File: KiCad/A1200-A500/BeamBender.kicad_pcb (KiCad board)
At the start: 4 copper layers, 50 x 100 mm, 82 parts, among them J1 4-1734742-0, J2 HDMI_A_1.4, J3 STX-3501-3N, J4 Phoenix_Contact, J5 Conn_01x01, J6 Conn_02x06_Odd_Even, U1 LM1117-3.3, U2 GW1NR-UV9LQ144P, U3 ADV7513BSWZ, U4 MCP1702T-1802E_CB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

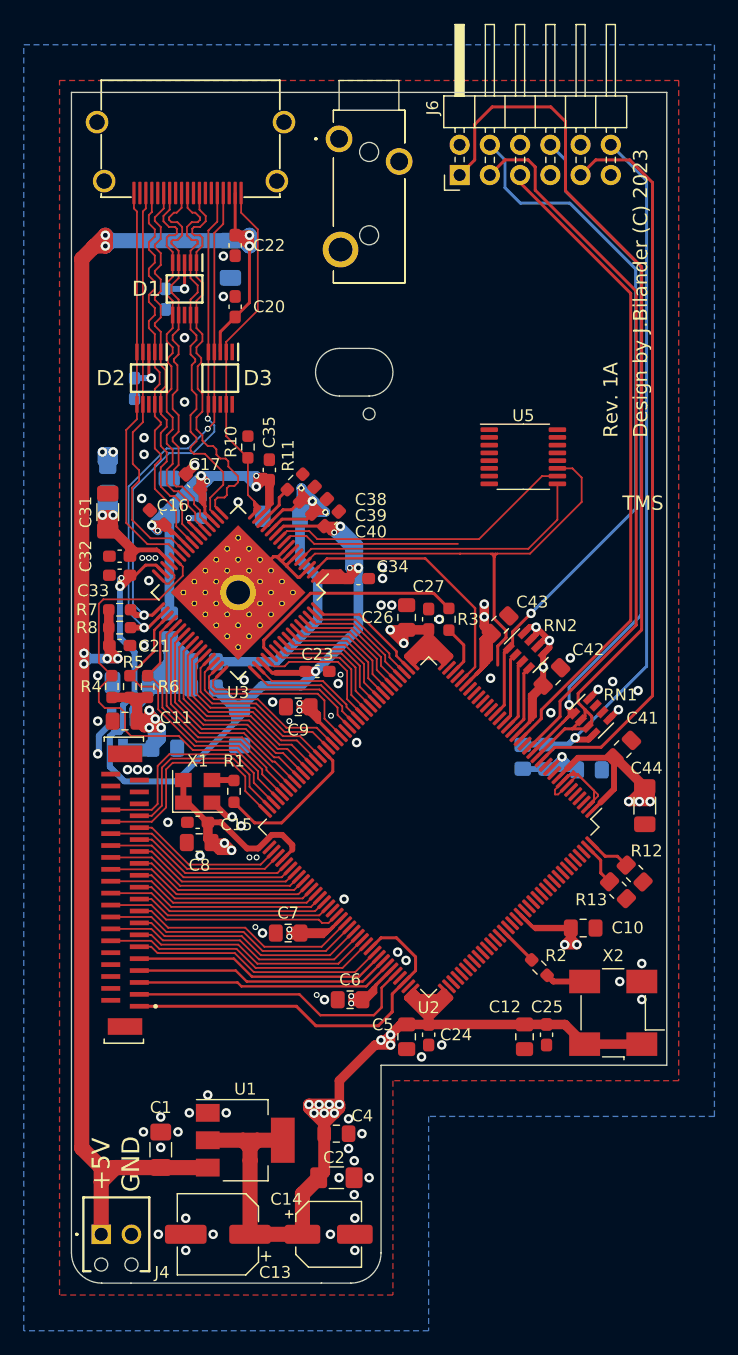
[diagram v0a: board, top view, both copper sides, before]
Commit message: added a 24.576 MHz crystal oscillator 5.0x3.2mm for Audio MCLK routed to FPGA pin 98 (GCLKT_2)
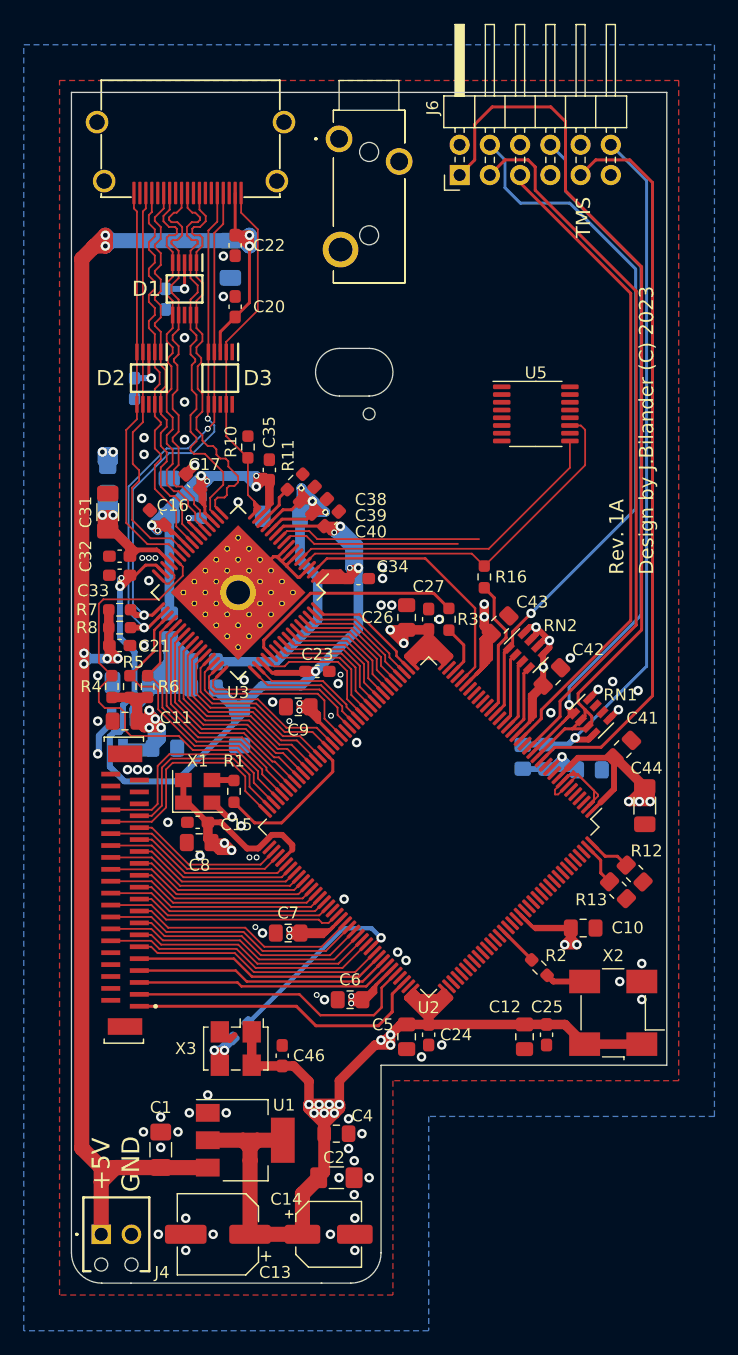
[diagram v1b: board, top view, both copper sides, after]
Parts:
- added C46: 0.01uF (0603), Capacitor_SMD:C_0603_1608Metric_Pad1.08x0.95mm_HandSolder, F.Cu at (115.8, 121.1)
- added R15: 22, Resistor_SMD:R_0603_1608Metric_Pad0.98x0.95mm_HandSolder, B.Cu at (112.3, 119.0)
- added R16: 22, Resistor_SMD:R_0603_1608Metric_Pad0.98x0.95mm_HandSolder, F.Cu at (132.8, 80.9)
- added X3: 5.0x3.2mm, Oscillator:Oscillator_SMD_TXC_7C-4Pin_5.0x3.2mm_HandSoldering, F.Cu at (111.9, 120.5)
- moved U5 3.75 mm to (137.1, 67.2)
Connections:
- U2 pad 98: C14M_3V3 -> XTAL_24.576M
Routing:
- net XTAL_24.576M: track 0.00 -> 16.0 mm, vias 0 -> 1
- net Net-(R16-Pad1): track 0.00 -> 11.5 mm
- net 3V3: track 296.1 -> 306.2 mm
- net LRCLK: track 26.0 -> 17.3 mm
- net MCLK: track 40.8 -> 32.2 mm
- net Net-(R15-Pad1): track 0.00 -> 7.48 mm, vias 0 -> 2
- net C14M_3V3: track 32.7 -> 25.3 mm
- net I2S0: track 25.9 -> 28.0 mm
- net GND: track 38.8 -> 39.5 mm, vias 76 -> 75

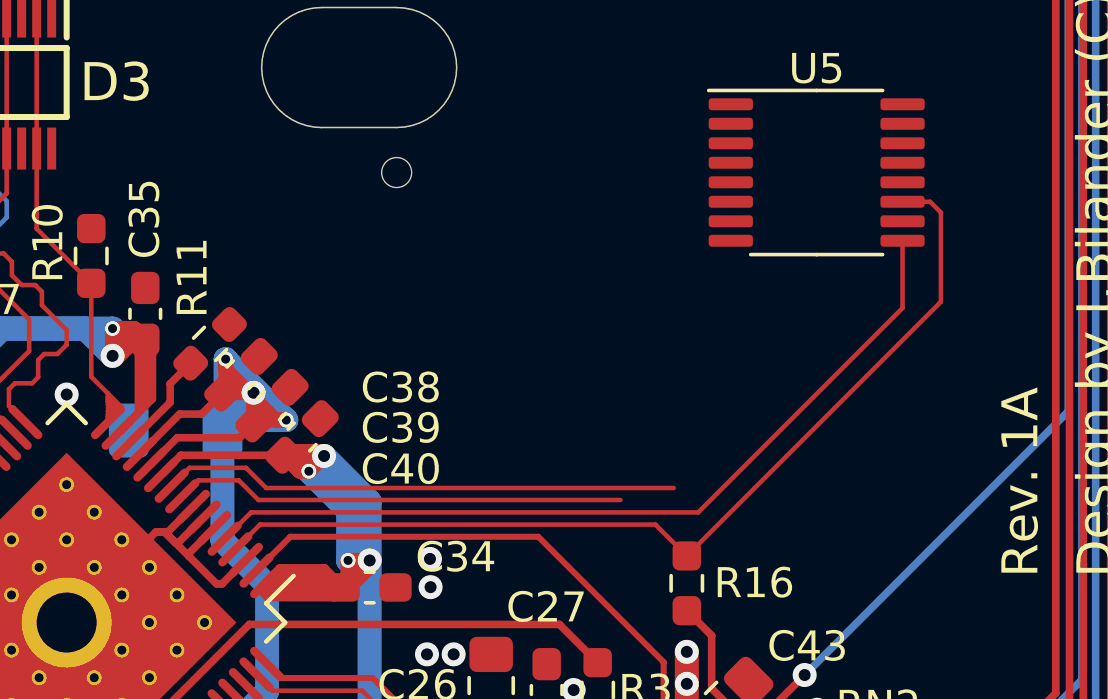
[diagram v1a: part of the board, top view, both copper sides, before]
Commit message: Added series resistors to BCLK, LRCLK and I2S0 audio lines.
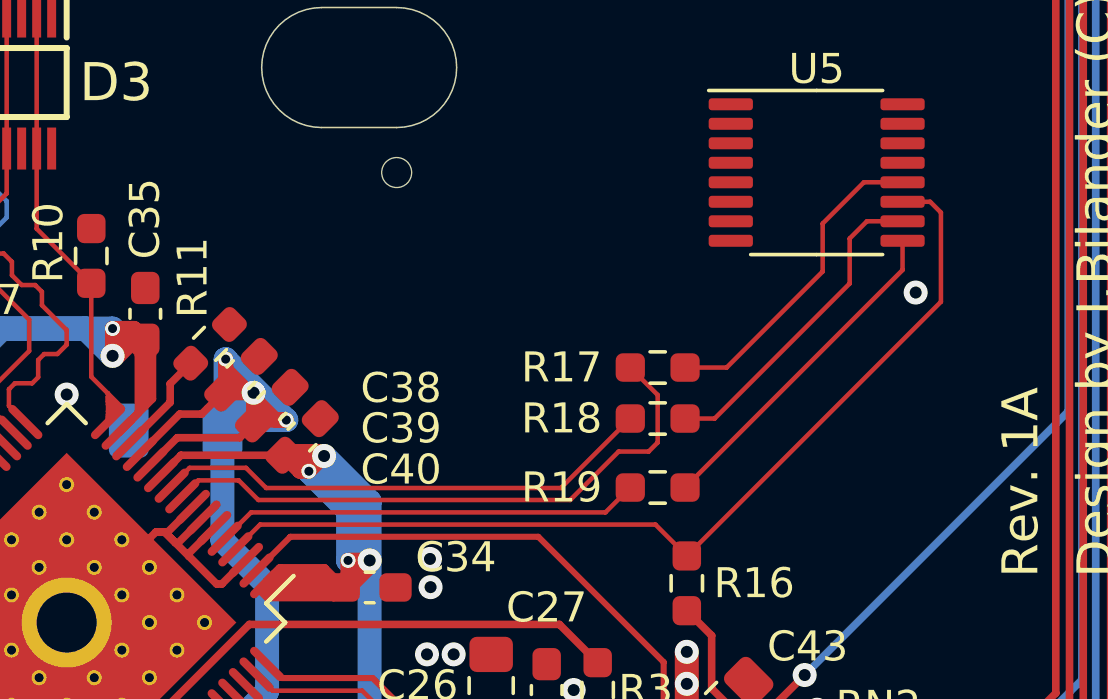
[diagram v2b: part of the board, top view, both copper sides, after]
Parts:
- added R17: 22, Resistor_SMD:R_0603_1608Metric_Pad0.98x0.95mm_HandSolder, F.Cu at (131.8, 73.7)
- added R18: 22, Resistor_SMD:R_0603_1608Metric_Pad0.98x0.95mm_HandSolder, F.Cu at (131.8, 75.4)
- added R19: 22, Resistor_SMD:R_0603_1608Metric_Pad0.98x0.95mm_HandSolder, F.Cu at (131.8, 77.7)
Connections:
- U5 pad 10: LRCLK -> Net-(R18-Pad1)
- U5 pad 12: BCLK -> Net-(R17-Pad1)
- U5 pad 9: I2S0 -> Net-(R19-Pad1)
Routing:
- net I2S0: track 28.0 -> 14.2 mm
- net Net-(R19-Pad1): track 0.00 -> 11.2 mm
- net Net-(R18-Pad1): track 0.00 -> 10.9 mm
- net Net-(R17-Pad1): track 0.00 -> 10.7 mm
- net BCLK: track 15.1 -> 20.0 mm
- net GND: vias 75 -> 76

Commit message: assigned the audio Left and Right channels to 3.5mm phono jack (STX-3501-3N) and to ADC-chip (AK5720)
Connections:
- J3 pad 1: L_AUDIO -> GND
- J3 pad 2: R_AUDIO -> L_AUDIO
- J3 pad 3: GND -> R_AUDIO
- U5 pad 2: Net-(U5-Pad2) -> R_AUDIO
- U5 pad 3: Net-(U5-Pad3) -> L_AUDIO

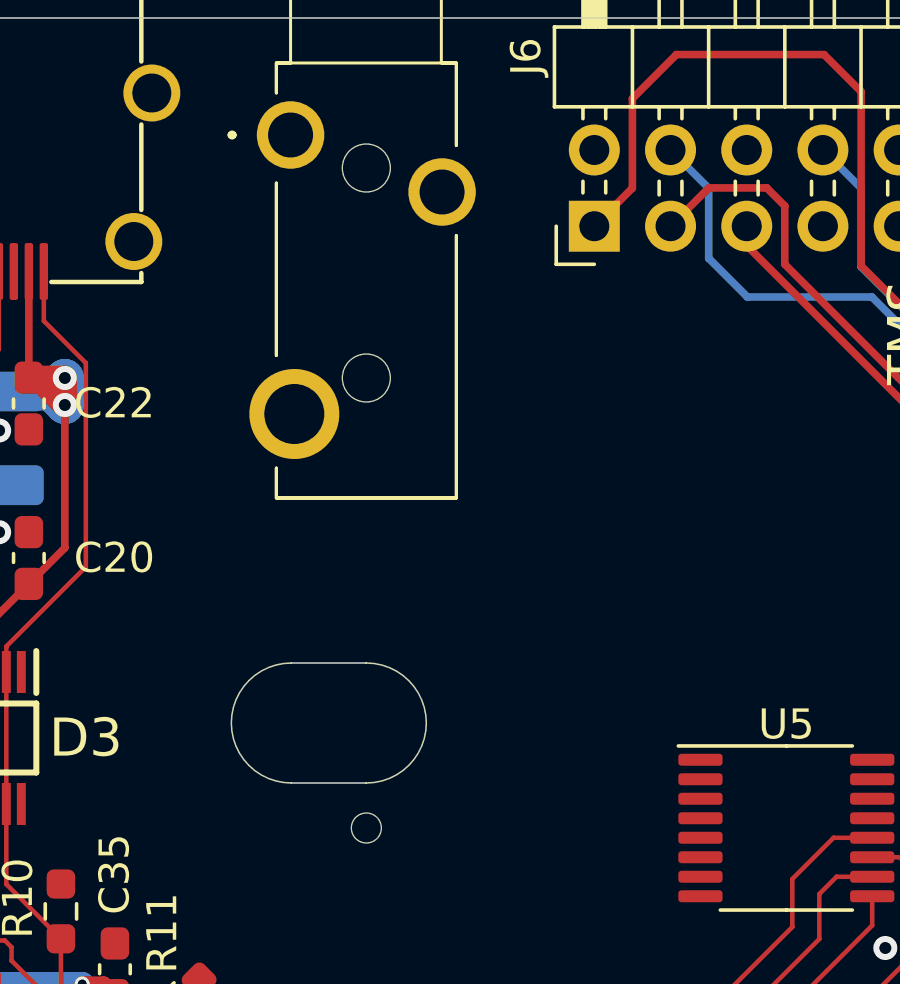
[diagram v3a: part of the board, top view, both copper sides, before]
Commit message: Added coupling caps for analogue left and right channel to inputs on ADC-chip (AK5720VT)
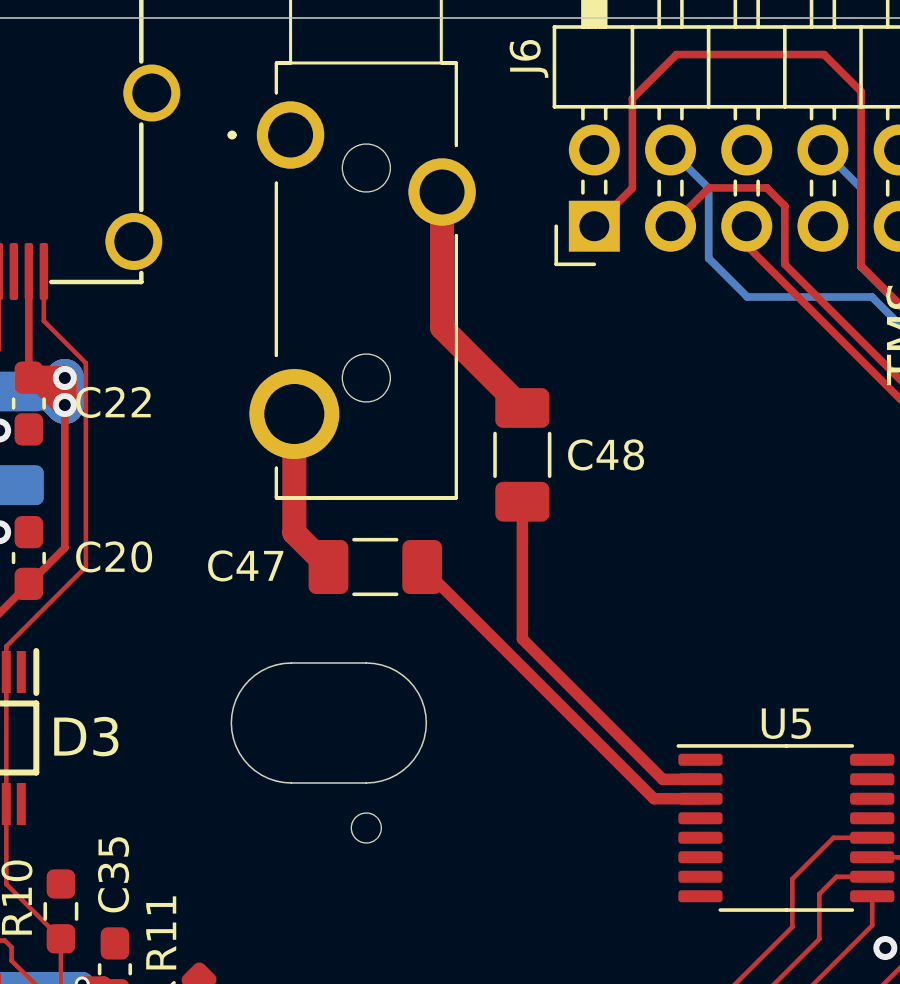
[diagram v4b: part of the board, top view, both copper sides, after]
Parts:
- added C47: 10uF (1206), Capacitor_SMD:C_1206_3216Metric_Pad1.33x1.80mm_HandSolder, F.Cu at (123.4, 58.5)
- added C48: 10uF (1206), Capacitor_SMD:C_1206_3216Metric_Pad1.33x1.80mm_HandSolder, F.Cu at (128.3, 54.8)
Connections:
- U5 pad 2: R_AUDIO -> Net-(C48-Pad2)
- U5 pad 3: L_AUDIO -> Net-(C47-Pad2)
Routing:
- net Net-(C47-Pad2): track 0.00 -> 12.5 mm
- net Net-(C48-Pad2): track 0.00 -> 12.4 mm
- net R_AUDIO: track 0.00 -> 8.31 mm
- net L_AUDIO: track 0.00 -> 5.57 mm

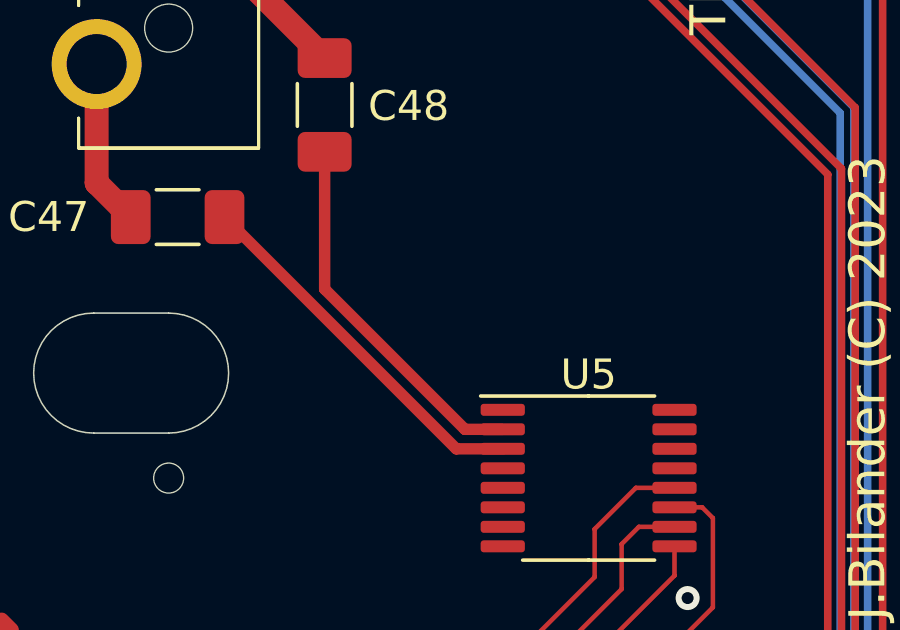
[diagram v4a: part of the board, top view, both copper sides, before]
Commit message: Added a 0.47uF cap for ADC-chip VCOM pin (Voltage Reference)
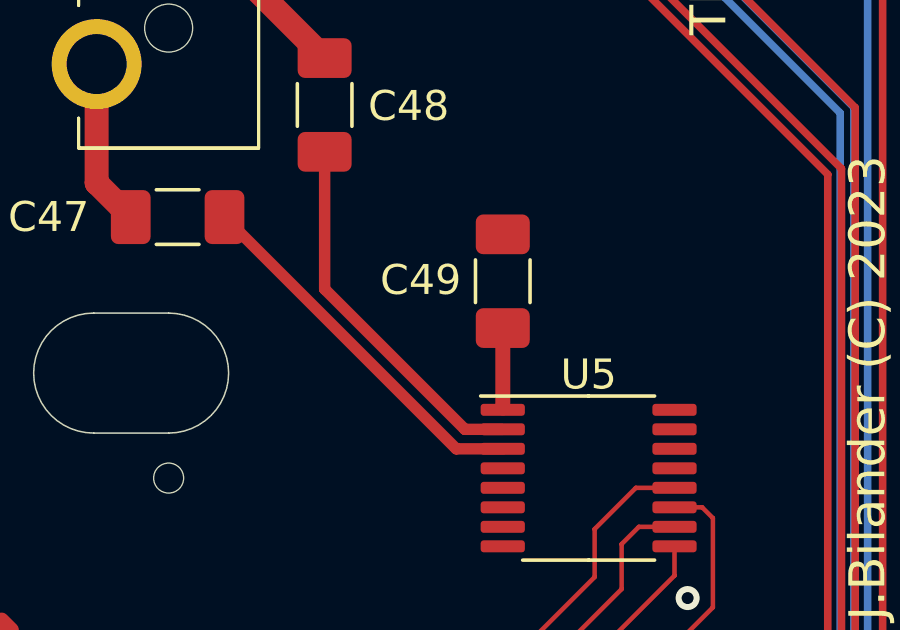
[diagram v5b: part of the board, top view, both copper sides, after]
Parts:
- added C49: 0.47uF (1206), Capacitor_SMD:C_1206_3216Metric_Pad1.33x1.80mm_HandSolder, F.Cu at (134.2, 60.7)
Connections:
- U5 pad 1: Net-(U5-Pad1) -> /BeamBender_FPGA/VCOM
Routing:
- net /BeamBender_FPGA/VCOM: track 0.00 -> 2.72 mm

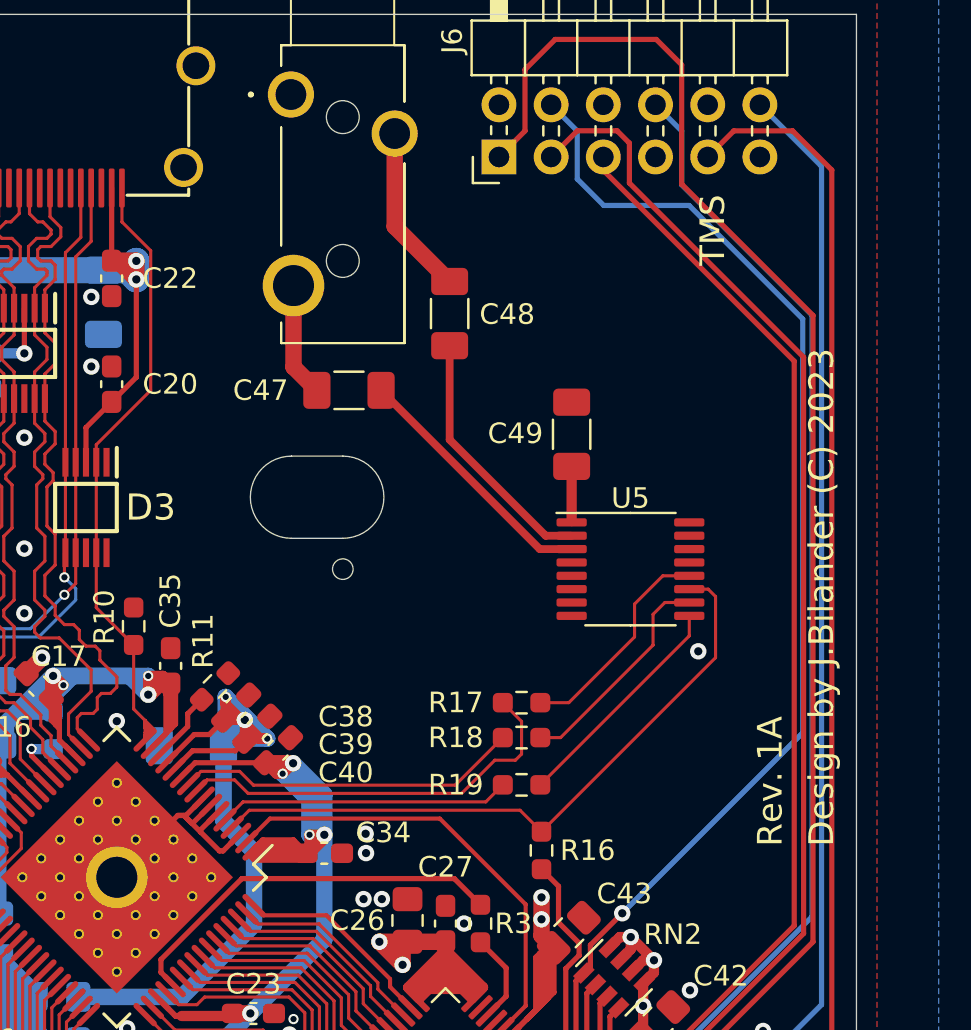
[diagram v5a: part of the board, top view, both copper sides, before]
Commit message: Repositioning of the AK5720 chip and routed the analog supply with 5V and digital supply with 3V3
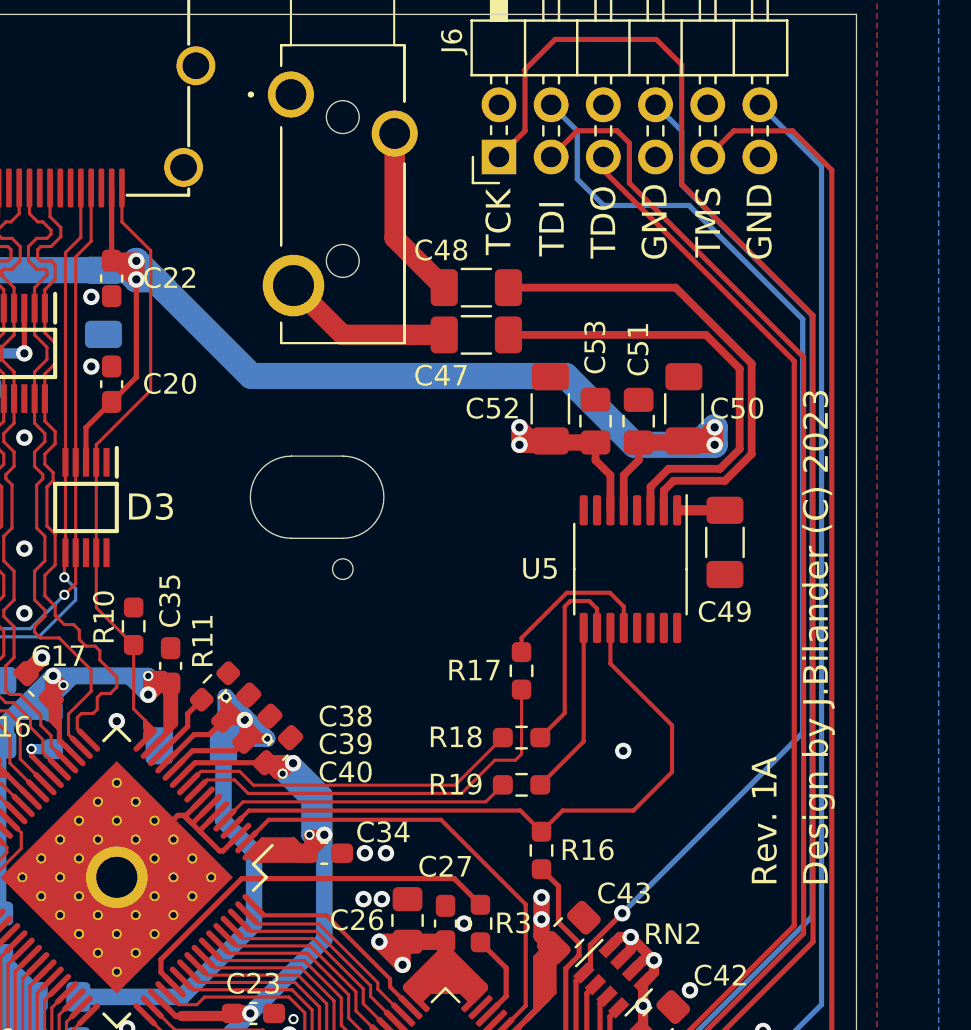
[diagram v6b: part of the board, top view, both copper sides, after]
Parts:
- added C50: 10uF (1206), Capacitor_SMD:C_1206_3216Metric_Pad1.33x1.80mm_HandSolder, F.Cu at (139.7, 59.4)
- added C51: 0.1uF (0805), Capacitor_SMD:C_0805_2012Metric_Pad1.18x1.45mm_HandSolder, F.Cu at (137.5, 60.0)
- added C52: 10uF (1206), Capacitor_SMD:C_1206_3216Metric_Pad1.33x1.80mm_HandSolder, F.Cu at (133.2, 59.4)
- added C53: 0.1uF (0805), Capacitor_SMD:C_0805_2012Metric_Pad1.18x1.45mm_HandSolder, F.Cu at (135.4, 60.0)
- moved C49 9.13 mm to (141.7, 65.9), turned to 90 degrees
- moved C47 6.76 mm to (129.6, 55.8)
- moved C48 1.81 mm to (129.6, 53.5), turned to 0 degrees
- moved R17 1.55 mm to (131.8, 72.2), turned to 270 degrees
- turned U5 to 270 degrees
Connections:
- U5 pad 5: Net-(U5-Pad5) -> VCC
- U5 pad 6: Net-(U5-Pad6) -> 3V3
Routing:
- net VCC: track 145.6 -> 191.1 mm, vias 8 -> 10
- net Net-(C48-Pad2): track 12.4 -> 23.7 mm
- net 3V3: track 306.2 -> 316.3 mm, vias 39 -> 41
- net Net-(C47-Pad2): track 12.5 -> 22.1 mm
- net Net-(R17-Pad1): track 10.7 -> 7.89 mm
- net L_AUDIO: track 5.57 -> 8.33 mm
- net Net-(R19-Pad1): track 11.2 -> 8.51 mm
- net Net-(R18-Pad1): track 10.9 -> 9.64 mm
- net MCLK: track 32.2 -> 31.6 mm
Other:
- board text added: "TCK"
- board text added: "TDI"
- board text added: "TDO"
